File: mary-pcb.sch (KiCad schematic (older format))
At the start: 1 part

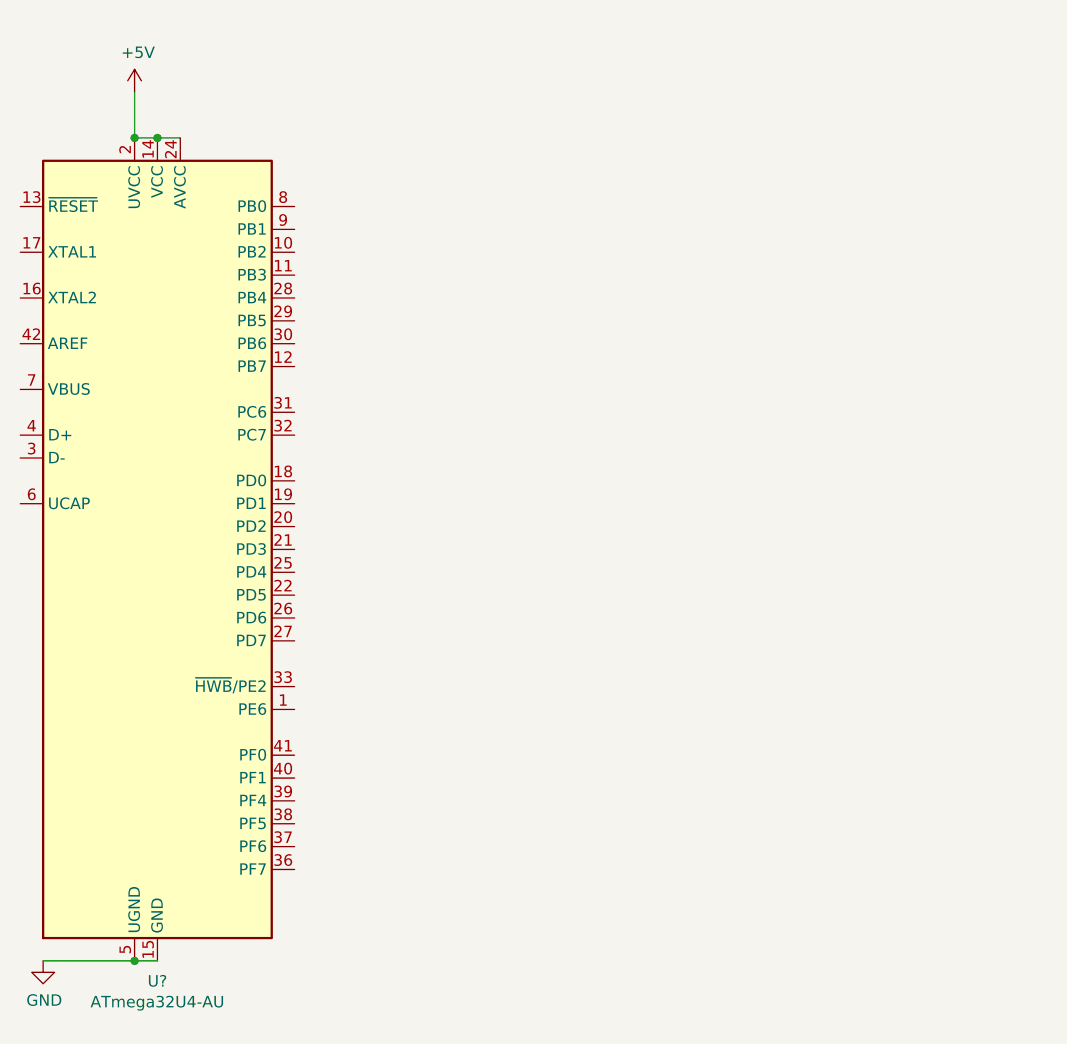
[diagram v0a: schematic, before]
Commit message: add MCU to schematic
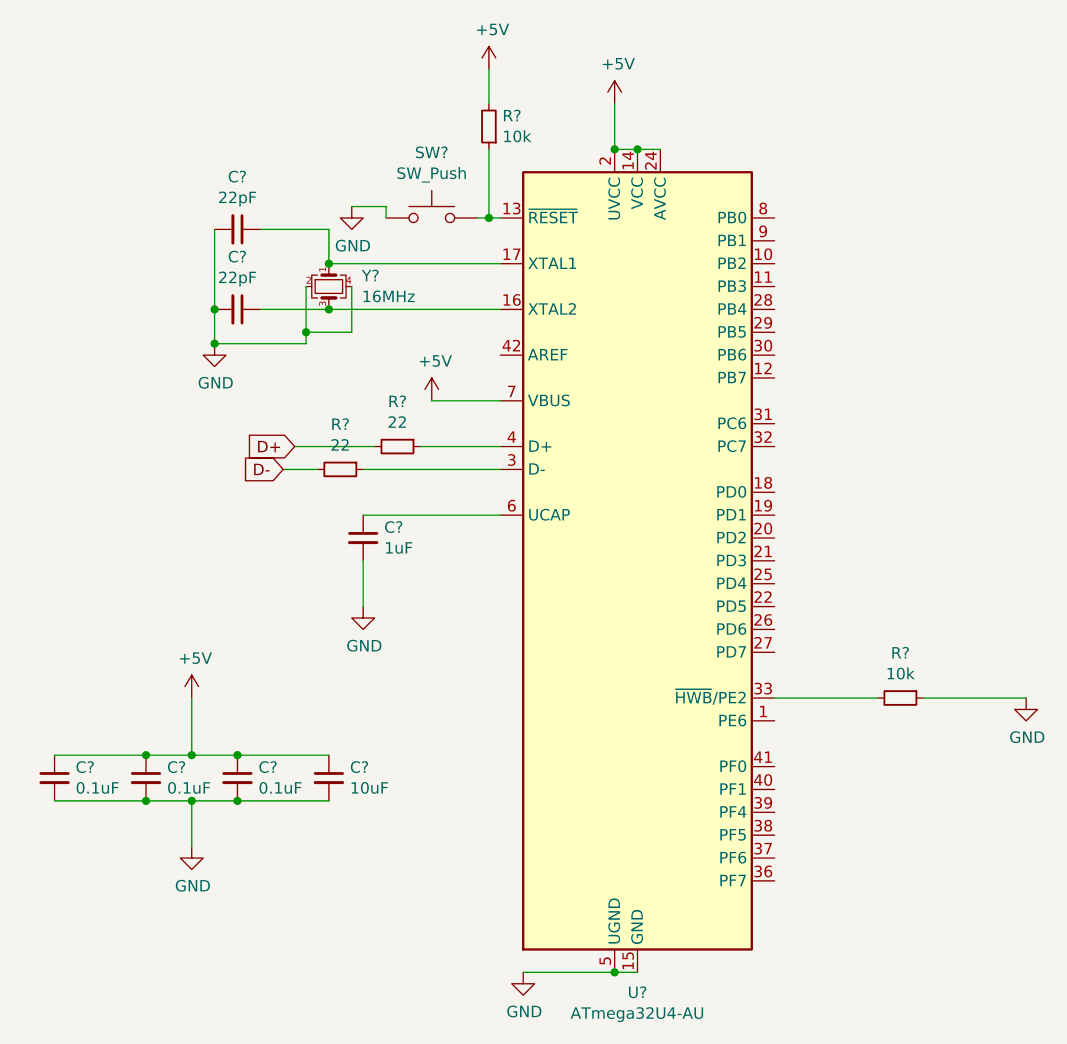
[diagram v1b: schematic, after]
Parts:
- added C?: 1uF, symbol Device:C_Small
- added C? (x3): 0.1uF, symbol Device:C_Small
- added C?: 10uF, symbol Device:C_Small
- added C? (x2): 22pF, symbol Device:C_Small
- added R? (x2): 10k, symbol Device:R_Small
- added R? (x2): 22, symbol Device:R_Small
- added SW?: SW_Push, symbol Switch:SW_Push
- added Y?: 16MHz, symbol Device:Crystal_GND24_Small
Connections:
- net +5V: now also U?.7 (VBUS), C?.1, C?.1, C?.1, C?.1, R?.2
- net GND: now also C?.2, C?.2, C?.2, C?.2, C?.2, C?.2, C?.2, R?.1, SW?.1, Y?.2, Y?.4
- net at U?.13 (~RESET): now also R?.1, SW?.2
- net at U?.16 (XTAL2): now also C?.1, Y?.3
- net at U?.17 (XTAL1): now also C?.1, Y?.1
- net at U?.3 (D-): now also R?.1
- net at U?.33 (~HWB~/PE2): now also R?.2
- net at U?.4 (D+): now also R?.1
- net at U?.6 (UCAP): now also C?.1
- new net D+: R?.2
- new net D-: R?.2
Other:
- moved on the sheet: U?

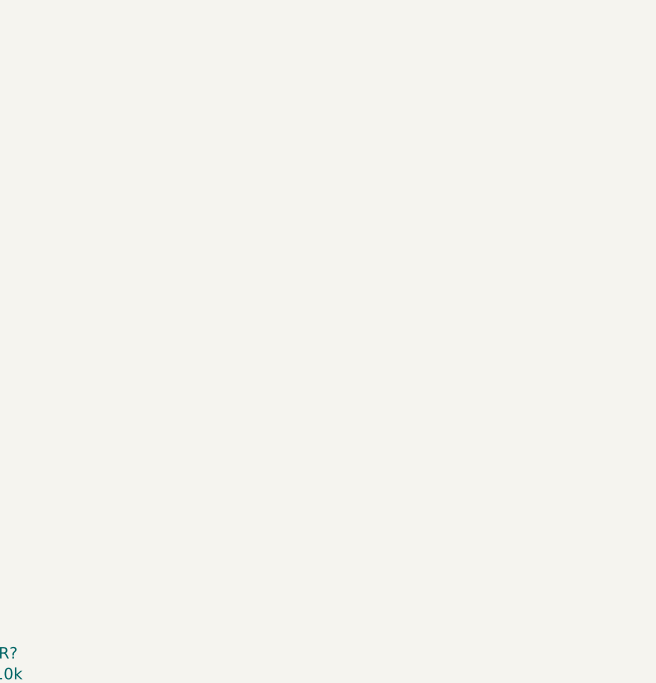
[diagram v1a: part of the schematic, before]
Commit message: add usb c to schematic
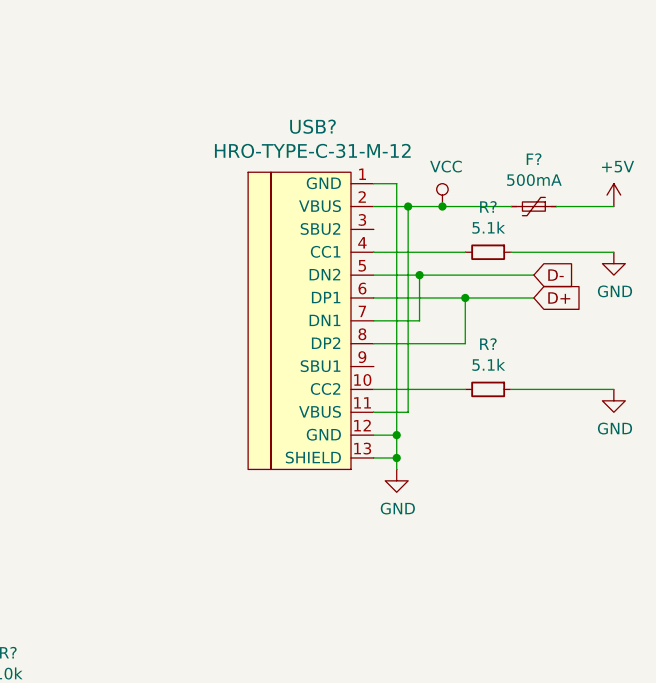
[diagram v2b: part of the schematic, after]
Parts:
- added F?: 500mA, symbol Device:Polyfuse_Small
- added R? (x2): 5.1k, symbol Device:R_Small
- added USB?: HRO-TYPE-C-31-M-12, symbol Type-C:HRO-TYPE-C-31-M-12
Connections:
- net +5V: now also F?.1
- net D+: now also USB?.6 (DP1), USB?.8 (DP2)
- net D-: now also USB?.5 (DN2), USB?.7 (DN1)
- net GND: now also R?.1, R?.1, USB?.1 (GND), USB?.12 (GND), USB?.13 (SHIELD)
- new net: R?.2, USB?.10 (CC2)
- new net: R?.2, USB?.4 (CC1)
- new net VCC: F?.2, USB?.11 (VBUS), USB?.2 (VBUS)
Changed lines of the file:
@@
 Text GLabel 3050 2850 0    50   Input ~ 0
 D-
+$Comp
+L Type-C:HRO-TYPE-C-31-M-12 USB?
+U 1 1 5E154775
+P 7250 2150
+F 0 "USB?" H 7083 2947 60  0000 C CNN
+F 1 "HRO-TYPE-C-31-M-12" H 7083 2841 60  0000 C CNN
+F 2 "" H 7250 2150 60  0001 C CNN
+F 3 "" H 7250 2150 60  0001 C CNN
+	1    7250 2150
+	1    0    0    -1
+$EndComp
+$Comp
+L Device:Polyfuse_Small F?
+U 1 1 5E1567C4
+P 8050 1700
+F 0 "F?" V 7845 1700 50  0000 C CNN
+F 1 "500mA" V 7936 1700 50  0000 C CNN
+F 2 "" H 8100 1500 50  0001 L CNN
+F 3 "~" H 8050 1700 50  0001 C CNN
+	1    8050 1700
+	0    1    1    0
+$EndComp
+$Comp
+L power:+5V #PWR?
+U 1 1 5E15A63C
+P 8400 1700
+F 0 "#PWR?" H 8400 1550 50  0001 C CNN
+F 1 "+5V" H 8415 1873 50  0000 C CNN
+F 2 "" H 8400 1700 50  0001 C CNN
+F 3 "" H 8400 1700 50  0001 C CNN
+	1    8400 1700
+	1    0    0    -1
+$EndComp
+Wire Wire Line
+	7350 1700 7500 1700
+Wire Wire Line
+	8150 1700 8400 1700
+$Comp
+L power:VCC #PWR?
+U 1 1 5E15C909
+P 7650 1700
+F 0 "#PWR?" H 7650 1550 50  0001 C CNN
+F 1 "VCC" H 7667 1873 50  0000 C CNN
+F 2 "" H 7650 1700 50  0001 C CNN
+F 3 "" H 7650 1700 50  0001 C CNN
+	1    7650 1700
+	1    0    0    -1
+$EndComp
+Connection ~ 7650 1700
+Wire Wire Line
+	7650 1700 7950 1700
+Text GLabel 8050 2100 2    50   Input ~ 0
+D+
+Wire Wire Line
+	7350 2100 7750 2100
+Wire Wire Line
+	7350 2300 7750 2300
+Wire Wire Line
+	7750 2300 7750 2100
+Connection ~ 7750 2100
+Wire Wire Line
+	7750 2100 8050 2100
+Text GLabel 8050 2000 2    50   Input ~ 0
+D-
+Wire Wire Line
+	7350 2000 7550 2000
+Wire Wire Line
+	7350 2200 7550 2200
+Wire Wire Line
+	7550 2200 7550 2000
+Connection ~ 7550 2000
+Wire Wire Line
+	7550 2000 8050 2000
+$Comp
+L power:GND #PWR?
+U 1 1 5E164B62
+P 7450 2850
+F 0 "#PWR?" H 7450 2600 50  0001 C CNN
+F 1 "GND" H 7455 2677 50  0000 C CNN
+F 2 "" H 7450 2850 50  0001 C CNN
+F 3 "" H 7450 2850 50  0001 C CNN
+	1    7450 2850
+	1    0    0    -1
+$EndComp
+Wire Wire Line
+	7350 1600 7450 1600
+Wire Wire Line
+	7450 1600 7450 2700
+Wire Wire Line
+	7350 2700 7450 2700
+Connection ~ 7450 2700
+Wire Wire Line
+	7450 2700 7450 2800
+Wire Wire Line
+	7350 2800 7450 2800
+Connection ~ 7450 2800
+Wire Wire Line
+	7450 2800 7450 2850
+Wire Wire Line
+	7350 2600 7500 2600
+Wire Wire Line
+	7500 2600 7500 1700
+Connection ~ 7500 1700
+Wire Wire Line
+	7500 1700 7650 1700
+$Comp
+L power:GND #PWR?
+U 1 1 5E17016B
+P 8400 1900
+F 0 "#PWR?" H 8400 1650 50  0001 C CNN
+F 1 "GND" H 8405 1727 50  0000 C CNN
+F 2 "" H 8400 1900 50  0001 C CNN
+F 3 "" H 8400 1900 50  0001 C CNN
+	1    8400 1900
+	1    0    0    -1
+$EndComp
+$Comp
+L Device:R_Small R?
+U 1 1 5E172396
+P 7850 1900
+F 0 "R?" V 7654 1900 50  0000 C CNN
+F 1 "5.1k" V 7745 1900 50  0000 C CNN
+F 2 "" H 7850 1900 50  0001 C CNN
+F 3 "~" H 7850 1900 50  0001 C CNN
+	1    7850 1900
+	0    1    1    0
+$EndComp
+Wire Wire Line
+	7350 1900 7750 1900
+Wire Wire Line
+	7950 1900 8400 1900
+$Comp
+L Device:R_Small R?
+U 1 1 5E175B75
+P 7850 2500
+F 0 "R?" V 7654 2500 50  0000 C CNN
+F 1 "5.1k" V 7745 2500 50  0000 C CNN
+F 2 "" H 7850 2500 50  0001 C CNN
+F 3 "~" H 7850 2500 50  0001 C CNN
+	1    7850 2500
+	0    1    1    0
+$EndComp
+$Comp
+L power:GND #PWR?
+U 1 1 5E175EA6
+P 8400 2500
+F 0 "#PWR?" H 8400 2250 50  0001 C CNN
+F 1 "GND" H 8405 2327 50  0000 C CNN
+F 2 "" H 8400 2500 50  0001 C CNN
+F 3 "" H 8400 2500 50  0001 C CNN
+	1    8400 2500
+	1    0    0    -1
+$EndComp
+Wire Wire Line
+	7350 2500 7750 2500
+Wire Wire Line
+	7950 2500 8400 2500
 $EndSCHEMATC

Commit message: complete keyboard matrix
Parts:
- added D1, D10, D11, D12, D13, D14, D15, D16, D17, D18, D19, D2, D20, D21, D22, D23, D24, D3, D4, D5, D6, D7, D8, D9: D_Small, symbol Device:D_Small
- added MX1, MX10, MX11, MX12, MX13, MX14, MX15, MX16, MX17, MX18, MX19, MX2, MX20, MX21, MX22, MX23, MX24, MX25, MX26, MX3, MX4, MX5, MX6, MX7, MX8, MX9: MX-NoLED, symbol MX_Alps_Hybrid:MX-NoLED
- added SW2: Rotary_Encoder_Switch, symbol Device:Rotary_Encoder_Switch
- gave numbers to parts that had none: 18
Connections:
- net GND: now also SW2.C
- net Row5: now reaches U1.18 (PD0)
- net Row5: now also D21.1 (K), D22.1 (K), D23.1 (K), D24.1 (K)
- net Col0: now reaches U1.19 (PD1)
- net Col0: now also MX1.1 (COL), MX12.1 (COL), MX17.1 (COL), MX21.1 (COL), MX22.1 (COL), MX4.1 (COL), MX8.1 (COL)
- net Col1: now reaches U1.20 (PD2)
- net Col1: now also MX13.1 (COL), MX18.1 (COL), MX2.1 (COL), MX23.1 (COL), MX5.1 (COL), MX9.1 (COL)
- net Col2: now reaches U1.21 (PD3)
- net Col2: now also MX10.1 (COL), MX14.1 (COL), MX19.1 (COL), MX24.1 (COL), MX3.1 (COL), MX6.1 (COL)
- net A(Left?): now reaches U1.22 (PD5)
- net A(Left?): now also SW2.A
- net Col3: now reaches U1.25 (PD4)
- net Col3: now also MX11.1 (COL), MX15.1 (COL), MX16.1 (COL), MX20.1 (COL), MX25.1 (COL), MX26.1 (COL), MX7.1 (COL), SW2.S1
- net B(Right?): now reaches U1.26 (PD6)
- net B(Right?): now also SW2.B
- net Row0: now reaches U1.28 (PB4)
- net Row0: now also D1.1 (K), D2.1 (K), D3.1 (K), D4.1 (K)
- net Row1: now reaches U1.29 (PB5)
- net Row1: now also D5.1 (K), D6.1 (K), D7.1 (K), D8.1 (K)
- net Row2: now reaches U1.30 (PB6)
- net Row2: now also D10.1 (K), D11.1 (K), D12.1 (K), D9.1 (K)
- net Row3: now reaches U1.31 (PC6)
- net Row3: now also D13.1 (K), D14.1 (K), D15.1 (K), D16.1 (K)
- net Row4: now reaches U1.32 (PC7)
- net Row4: now also D17.1 (K), D18.1 (K), D19.1 (K), D20.1 (K)
- new net: D1.2 (A), MX1.2 (ROW)
- new net: D2.2 (A), MX2.2 (ROW)
- new net: D3.2 (A), MX3.2 (ROW)
- new net: D5.2 (A), MX4.2 (ROW)
- new net: D6.2 (A), MX5.2 (ROW)
- new net: D7.2 (A), MX6.2 (ROW)
- new net: D8.2 (A), MX7.2 (ROW)
- new net: D9.2 (A), MX8.2 (ROW)
- new net: D10.2 (A), MX9.2 (ROW)
- new net: D11.2 (A), MX10.2 (ROW)
- new net: D13.2 (A), MX12.2 (ROW)
- new net: D14.2 (A), MX13.2 (ROW)
- new net: D15.2 (A), MX14.2 (ROW)
- new net: D17.2 (A), MX17.2 (ROW)
- new net: D18.2 (A), MX18.2 (ROW)
- new net: D19.2 (A), MX19.2 (ROW)
- new net: D21.2 (A), MX21.2 (ROW), MX22.2 (ROW)
- new net: D23.2 (A), MX24.2 (ROW)
- new net: D20.2 (A), MX20.2 (ROW)
- new net: D22.2 (A), MX23.2 (ROW)
- new net: D12.2 (A), MX11.2 (ROW)
- new net: D16.2 (A), MX15.2 (ROW), MX16.2 (ROW)
- new net: D24.2 (A), MX25.2 (ROW), MX26.2 (ROW)
- new net: D4.2 (A), SW2.S2
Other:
- moved on the sheet: C1, C2, C3, C4, C5, C6, C7, F1, R1, R2, R3, R4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

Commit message: assign footprints
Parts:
- C1, C2, C3, C4, C5, C6, C7: footprint (none) -> Capacitor_SMD:C_0805_2012Metric
- D1, D10, D11, D12, D13, D14, D15, D16, D17, D18, D19, D2, D20, D21, D22, D23, D24, D3, D4, D5, D6, D7, D8, D9: footprint (none) -> Diode_SMD:D_SOD-123
- F1: footprint (none) -> Fuse:Fuse_1206_3216Metric
- MX1, MX10, MX11, MX12, MX13, MX14, MX15, MX17, MX18, MX19, MX2, MX20, MX22, MX23, MX24, MX25, MX3, MX4, MX5, MX6, MX7, MX8, MX9: footprint (none) -> MX_Alps_Hybrid:MX-1U-NoLED
- MX16, MX21, MX26: footprint (none) -> MX_Alps_Hybrid:MX-2U-ReversedStabilizers-NoLED
- R1, R2, R3, R4, R5, R6: footprint (none) -> Resistor_SMD:R_0805_2012Metric
- SW1: footprint (none) -> random-keyboard-parts:SKQG-1155865
- SW2: footprint (none) -> Keebio-Parts:RotaryEncoder_EC11
- USB1: footprint (none) -> Type-C:HRO-TYPE-C-31-M-12
- Y1: footprint (none) -> Crystal:Crystal_SMD_3225-4Pin_3.2x2.5mm

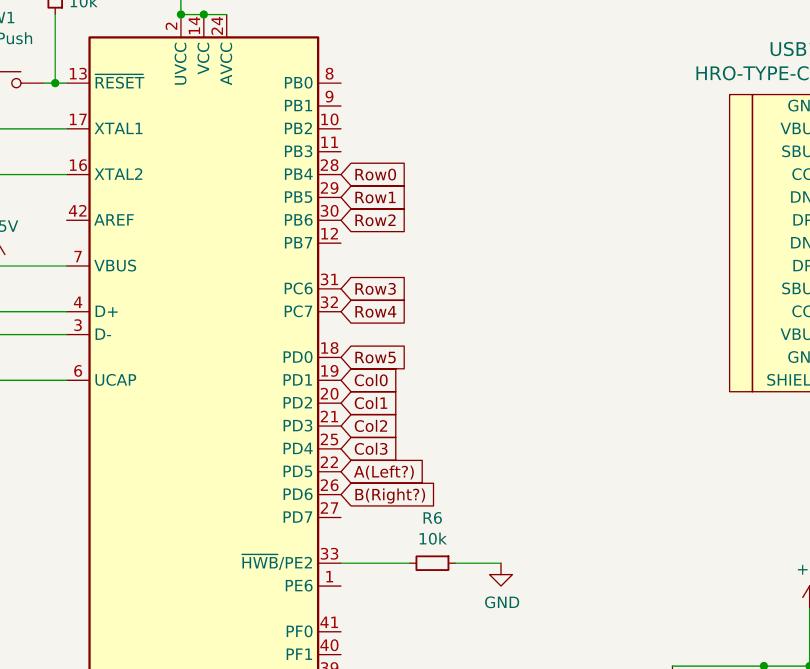
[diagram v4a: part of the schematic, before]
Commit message: place switches on pcb
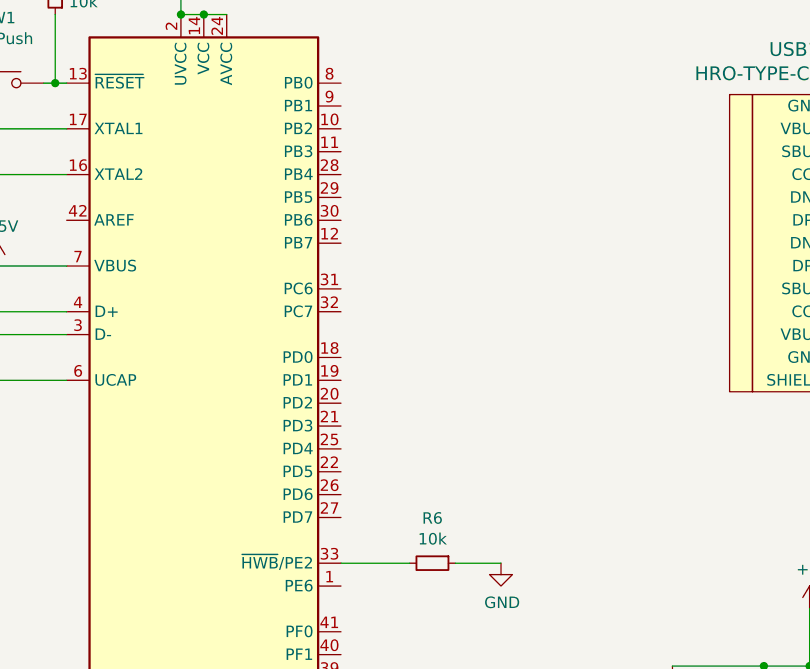
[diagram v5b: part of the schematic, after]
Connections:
- net A(Left?): no longer U1.22 (PD5)
- net B(Right?): no longer U1.26 (PD6)
- net Col0: no longer U1.19 (PD1)
- net Col1: no longer U1.20 (PD2)
- net Col2: no longer U1.21 (PD3)
- net Col3: no longer U1.25 (PD4)
- net Row0: no longer U1.28 (PB4)
- net Row1: no longer U1.29 (PB5)
- net Row2: no longer U1.30 (PB6)
- net Row3: no longer U1.31 (PC6)
- net Row4: no longer U1.32 (PC7)
- net Row5: no longer U1.18 (PD0)
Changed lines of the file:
@@
 Wire Wire Line
 	10450 700  10450 1350
-Text GLabel 3450 1850 2    50   Input ~ 0
-Row0
-Text GLabel 3450 1950 2    50   Input ~ 0
-Row1
-Text GLabel 3450 2050 2    50   Input ~ 0
-Row2
-Text GLabel 3450 2350 2    50   Input ~ 0
-Row3
-Text GLabel 3450 2450 2    50   Input ~ 0
-Row4
-Text GLabel 3450 2650 2    50   Input ~ 0
-Row5
-Text GLabel 3450 2750 2    50   Input ~ 0
-Col0
-Text GLabel 3450 2850 2    50   Input ~ 0
-Col1
-Text GLabel 3450 2950 2    50   Input ~ 0
-Col2
-Text GLabel 3450 3050 2    50   Input ~ 0
-Col3
-Text GLabel 3450 3150 2    50   Input ~ 0
-A(Left?)
-Text GLabel 3450 3250 2    50   Input ~ 0
-B(Right?)
 $EndSCHEMATC
